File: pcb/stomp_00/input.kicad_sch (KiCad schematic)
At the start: 2 parts, among them J15 Euro_Out_1, U2 TL072

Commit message: adding all the components...
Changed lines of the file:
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@@
 (kicad_sch (version 20230121) (generator eeschema)
   (paper "A4")
+  (text_box "Input stage, usually mono, instrument level up to line level."
+    (at 111.76 21.59 0) (size 50.8 20.32)
+    (stroke (width 0) (type default))
+    (fill (type none))
+    (effects (font (size 1.27 1.27)) (justify left top))
+  )
   (global_label "LINE_IN_R" (shape input) (at 135.89 63.5 0) (fields_autoplaced)
     (effects (font (size 1.27 1.27)) (justify left))

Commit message: taking shape...
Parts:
- U2: footprint (none) -> Package_SO:SOIC-8_3.9x4.9mm_P1.27mm
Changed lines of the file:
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@@
       (effects (font (size 1.27 1.27)))
     )
-    (property "Footprint" "" (at 86.995 64.77 0)
+    (property "Footprint" "Package_SO:SOIC-8_3.9x4.9mm_P1.27mm" (at 86.995 64.77 0)
       (effects (font (size 1.27 1.27)) hide)
     )
@@
       (effects (font (size 1.27 1.27)) (justify left))
     )
-    (property "Footprint" "" (at 88.9 84.455 0)
+    (property "Footprint" "Package_SO:SOIC-8_3.9x4.9mm_P1.27mm" (at 88.9 84.455 0)
       (effects (font (size 1.27 1.27)) hide)
     )
@@
       (effects (font (size 1.27 1.27)))
     )
-    (property "Footprint" "" (at 86.36 48.26 0)
+    (property "Footprint" "Package_SO:SOIC-8_3.9x4.9mm_P1.27mm" (at 86.36 48.26 0)
       (effects (font (size 1.27 1.27)) hide)
     )

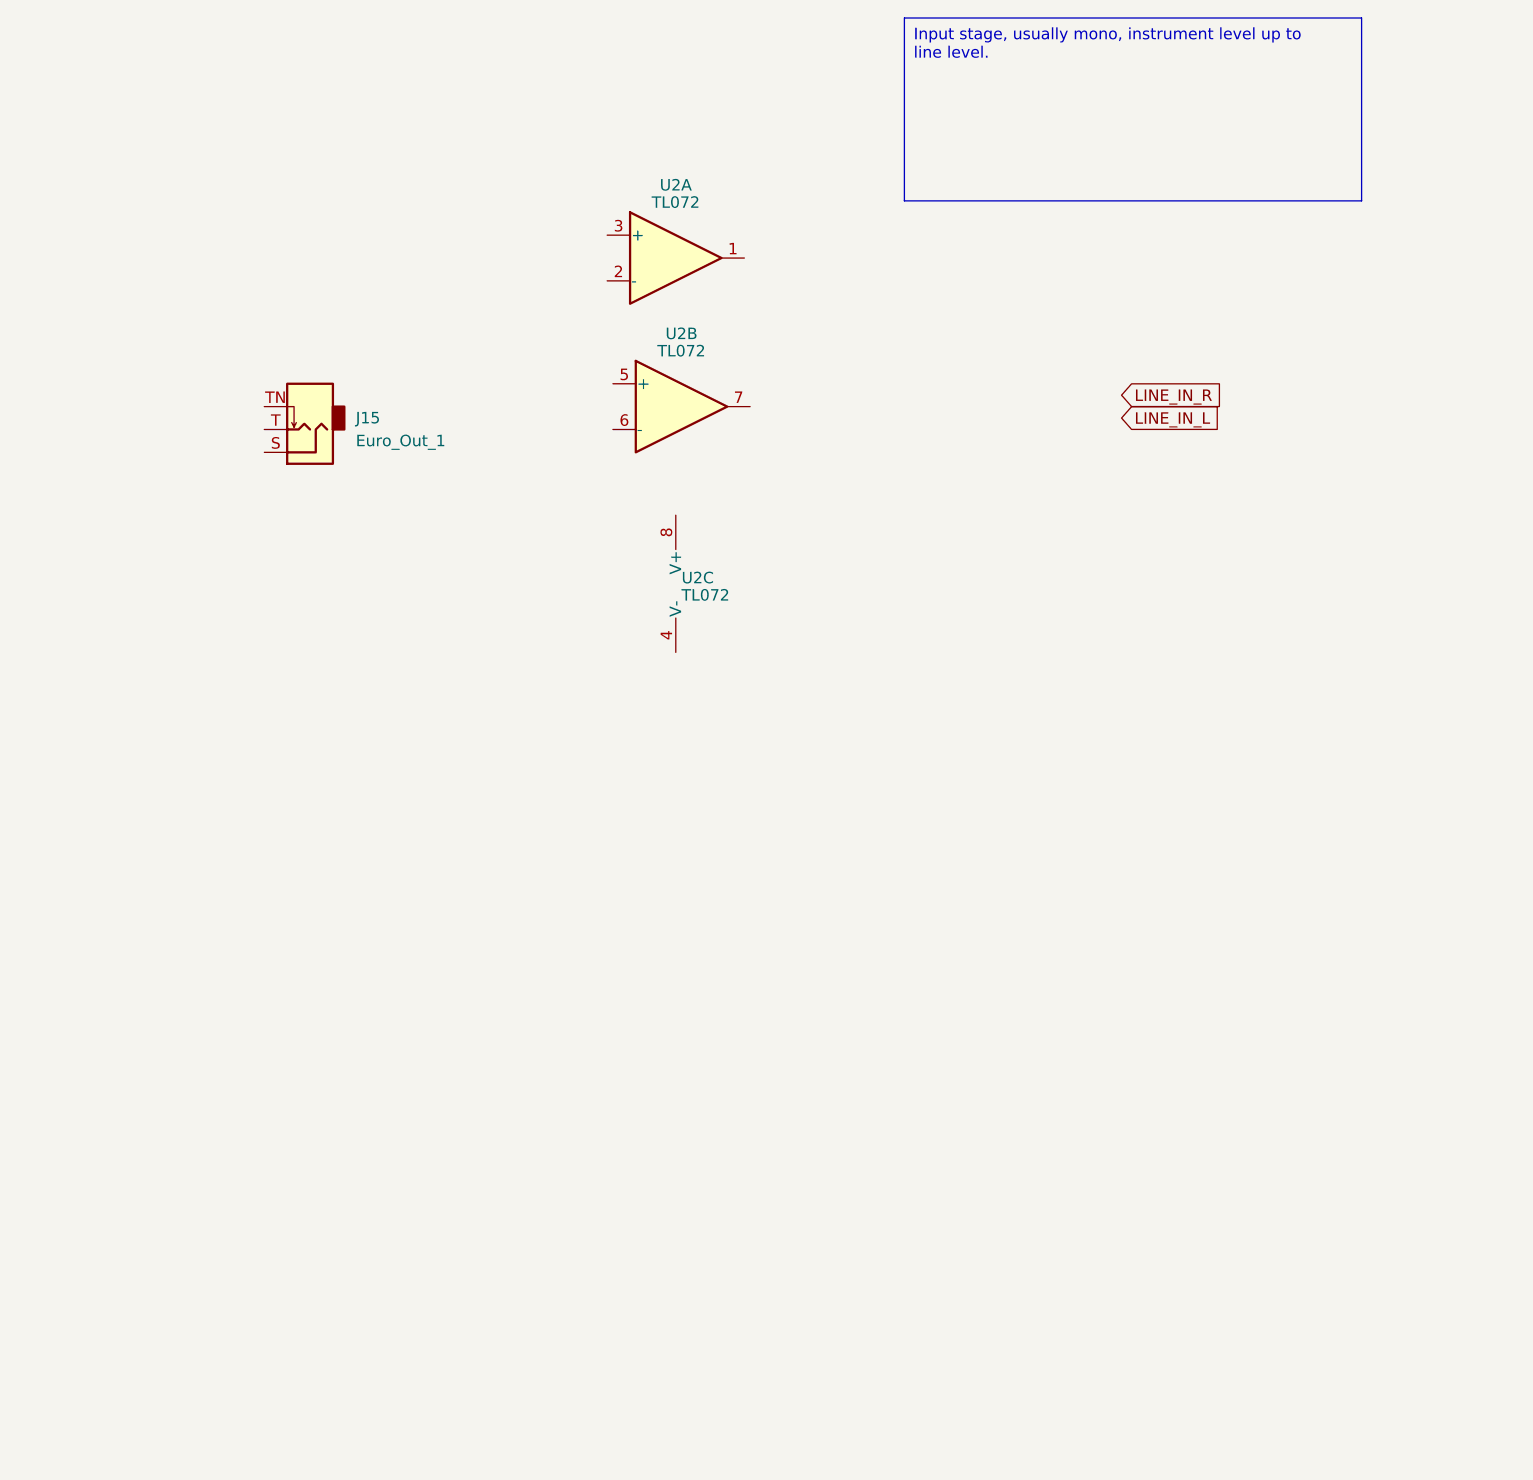
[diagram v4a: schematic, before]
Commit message: input stage schematic
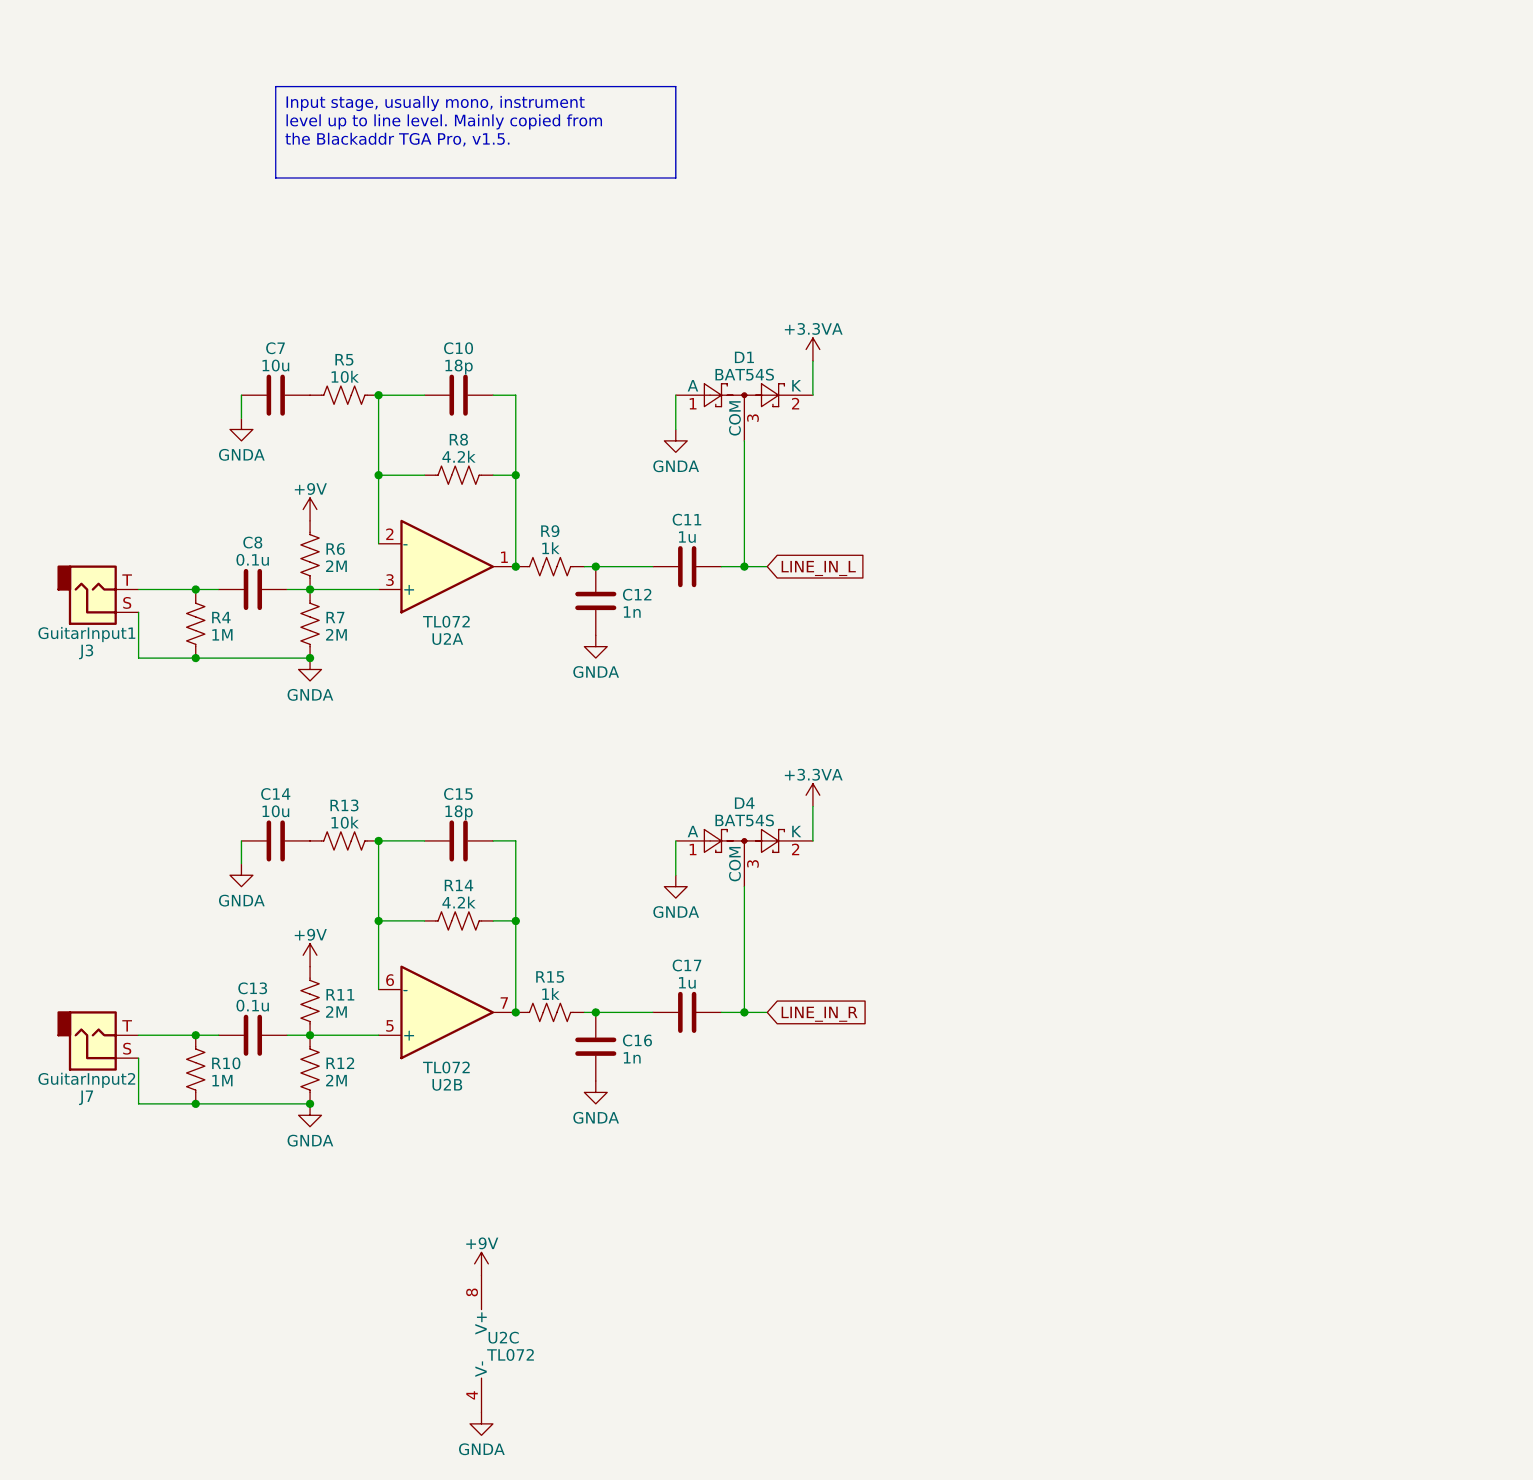
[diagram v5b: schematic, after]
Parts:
- removed J15: Euro_Out_1, AudioJacks:Jack_3.5mm_QingPu_WQP-PJ398SM_Vertical, symbol Connector_Audio:AudioJack2_SwitchT
- added C10, C15: 18p, symbol Device:C
- added C11, C17: 1u, symbol Device:C
- added C12, C16: 1n, symbol Device:C
- added C13, C8: 0.1u, symbol Device:C
- added C14, C7: 10u, symbol Device:C
- added D1, D4: BAT54S, Package_TO_SOT_SMD:SOT-23, symbol Diode:BAT54S
- added J3: GuitarInput1, symbol Connector_Audio:AudioJack2
- added J7: GuitarInput2, symbol Connector_Audio:AudioJack2
- added R10, R4: 1M, symbol Device:R_US
- added R11, R12, R6, R7: 2M, symbol Device:R_US
- added R13, R5: 10k, symbol Device:R_US
- added R14, R8: 4.2k, symbol Device:R_US
- added R15, R9: 1k, symbol Device:R_US
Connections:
- net LINE_IN_L: now also C11.1, D1.3 (COM)
- net LINE_IN_R: now also C17.1, D4.3 (COM)
- net at U2.5 (+): now also C13.2, R11.2, R12.1
- net at U2.6 (-): now also C15.1, R13.2, R14.1
- net at U2.7: now also C15.2, R14.2, R15.1
- net GNDA: now reaches U2.4 (V-)
- net GNDA: now also C12.2, C14.1, C16.2, C7.1, D1.1 (A), D4.1 (A), J3.S, J7.S, R10.2, R12.2, R4.2, R7.2
- net +9V: now reaches U2.8 (V+)
- net +9V: now also R11.1, R6.1
- net at U2.1: now also C10.2, R8.2, R9.1
- net at U2.2 (-): now also C10.1, R5.2, R8.1
- net at U2.3 (+): now also C8.2, R6.2, R7.1
- new net: C11.2, C12.1, R9.2
- new net: C14.2, R13.1
- new net: C7.2, R5.1
- new net: C16.1, C17.2, R15.2
- new net: C8.1, J3.T, R4.1
- new net: C13.1, J7.T, R10.1
- new net +3.3VA: D1.2 (K), D4.2 (K)
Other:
- moved on the sheet: U2A, U2B, U2C

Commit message: more input stage faffing
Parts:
- added C18: 100n, symbol Device:C
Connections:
- net +9V: now also C18.2
- net GNDA: now also C18.1
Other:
- note added: "Drain, prevents pop when switching to bypass"
- moved on the sheet: C10, C11, C12, C13, C14, C15, C16, C17, C7, C8, D1, D4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

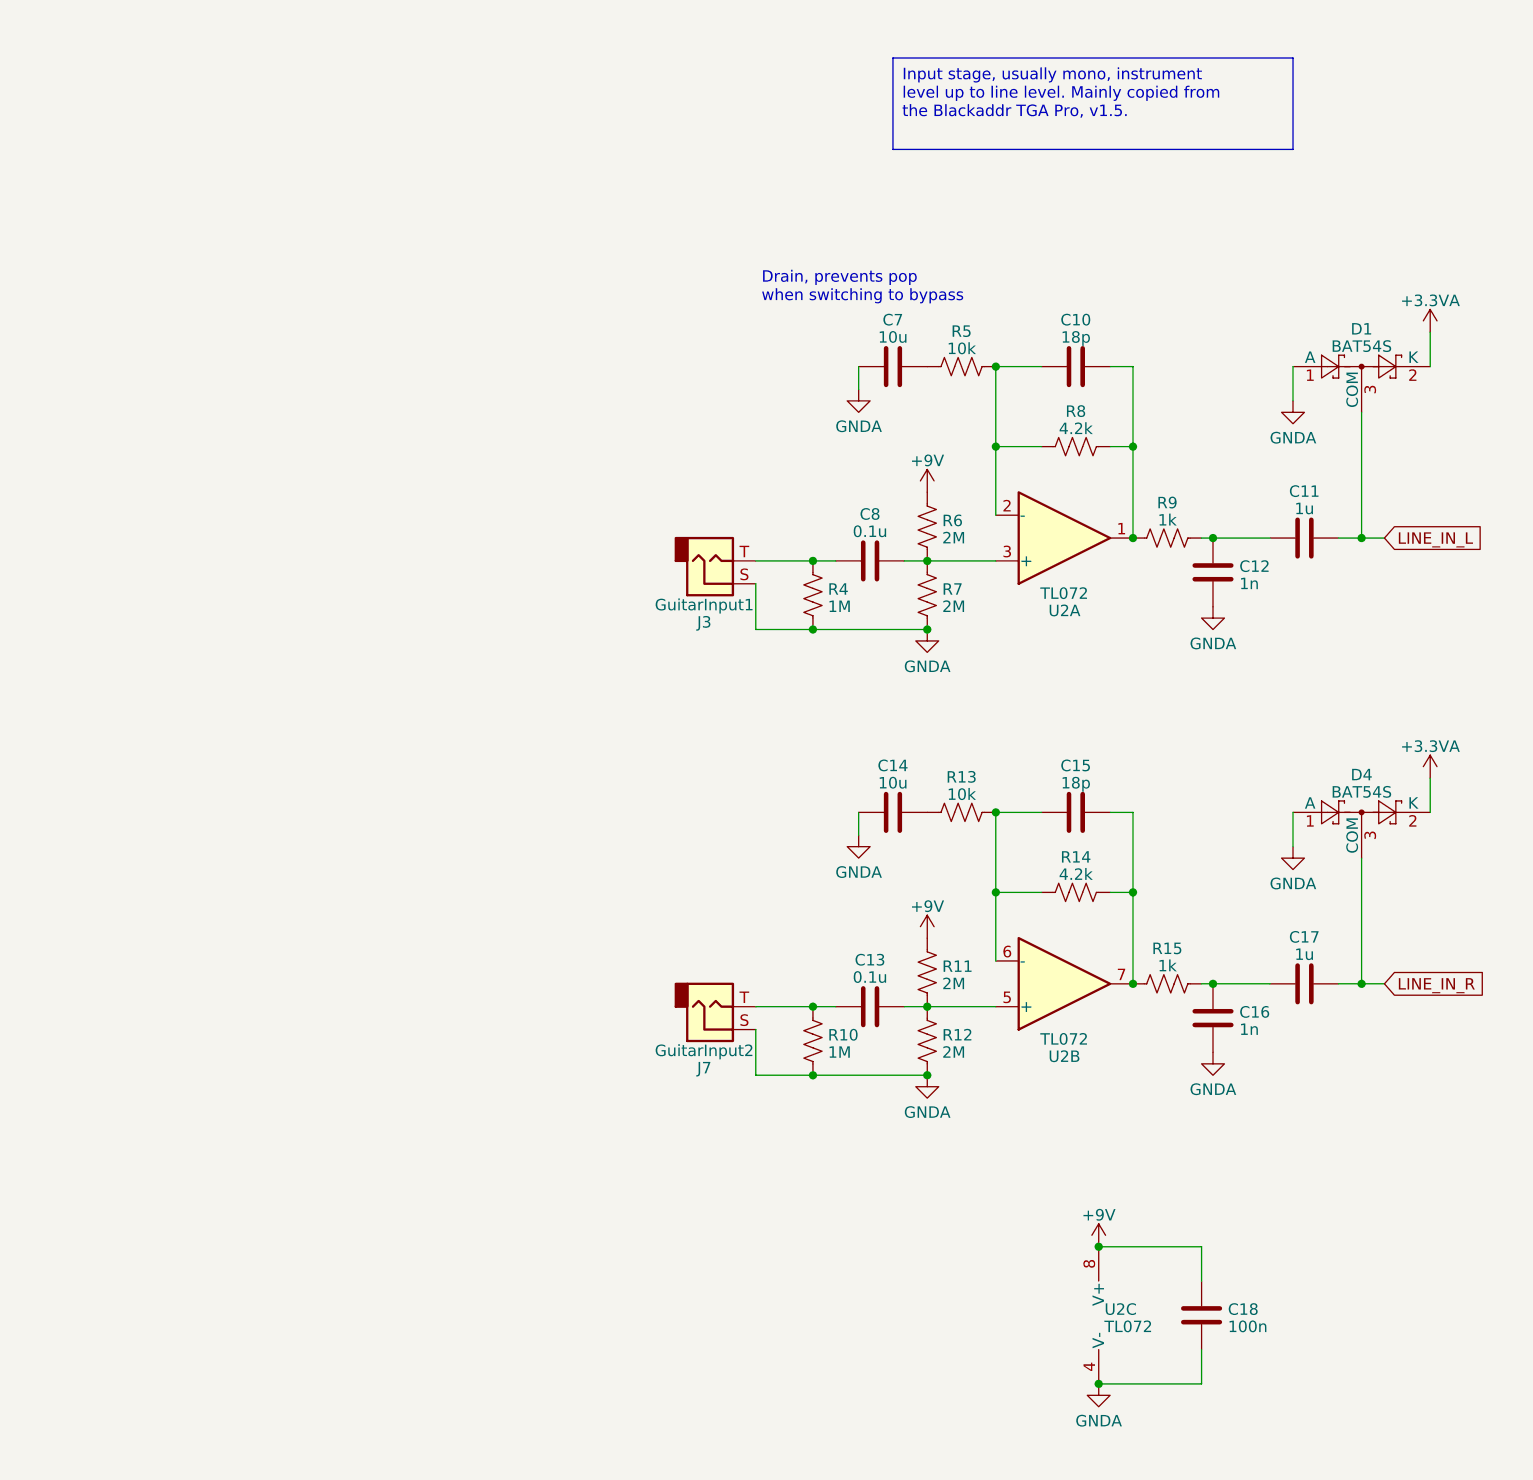
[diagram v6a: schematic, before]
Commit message: better layout in enclosure
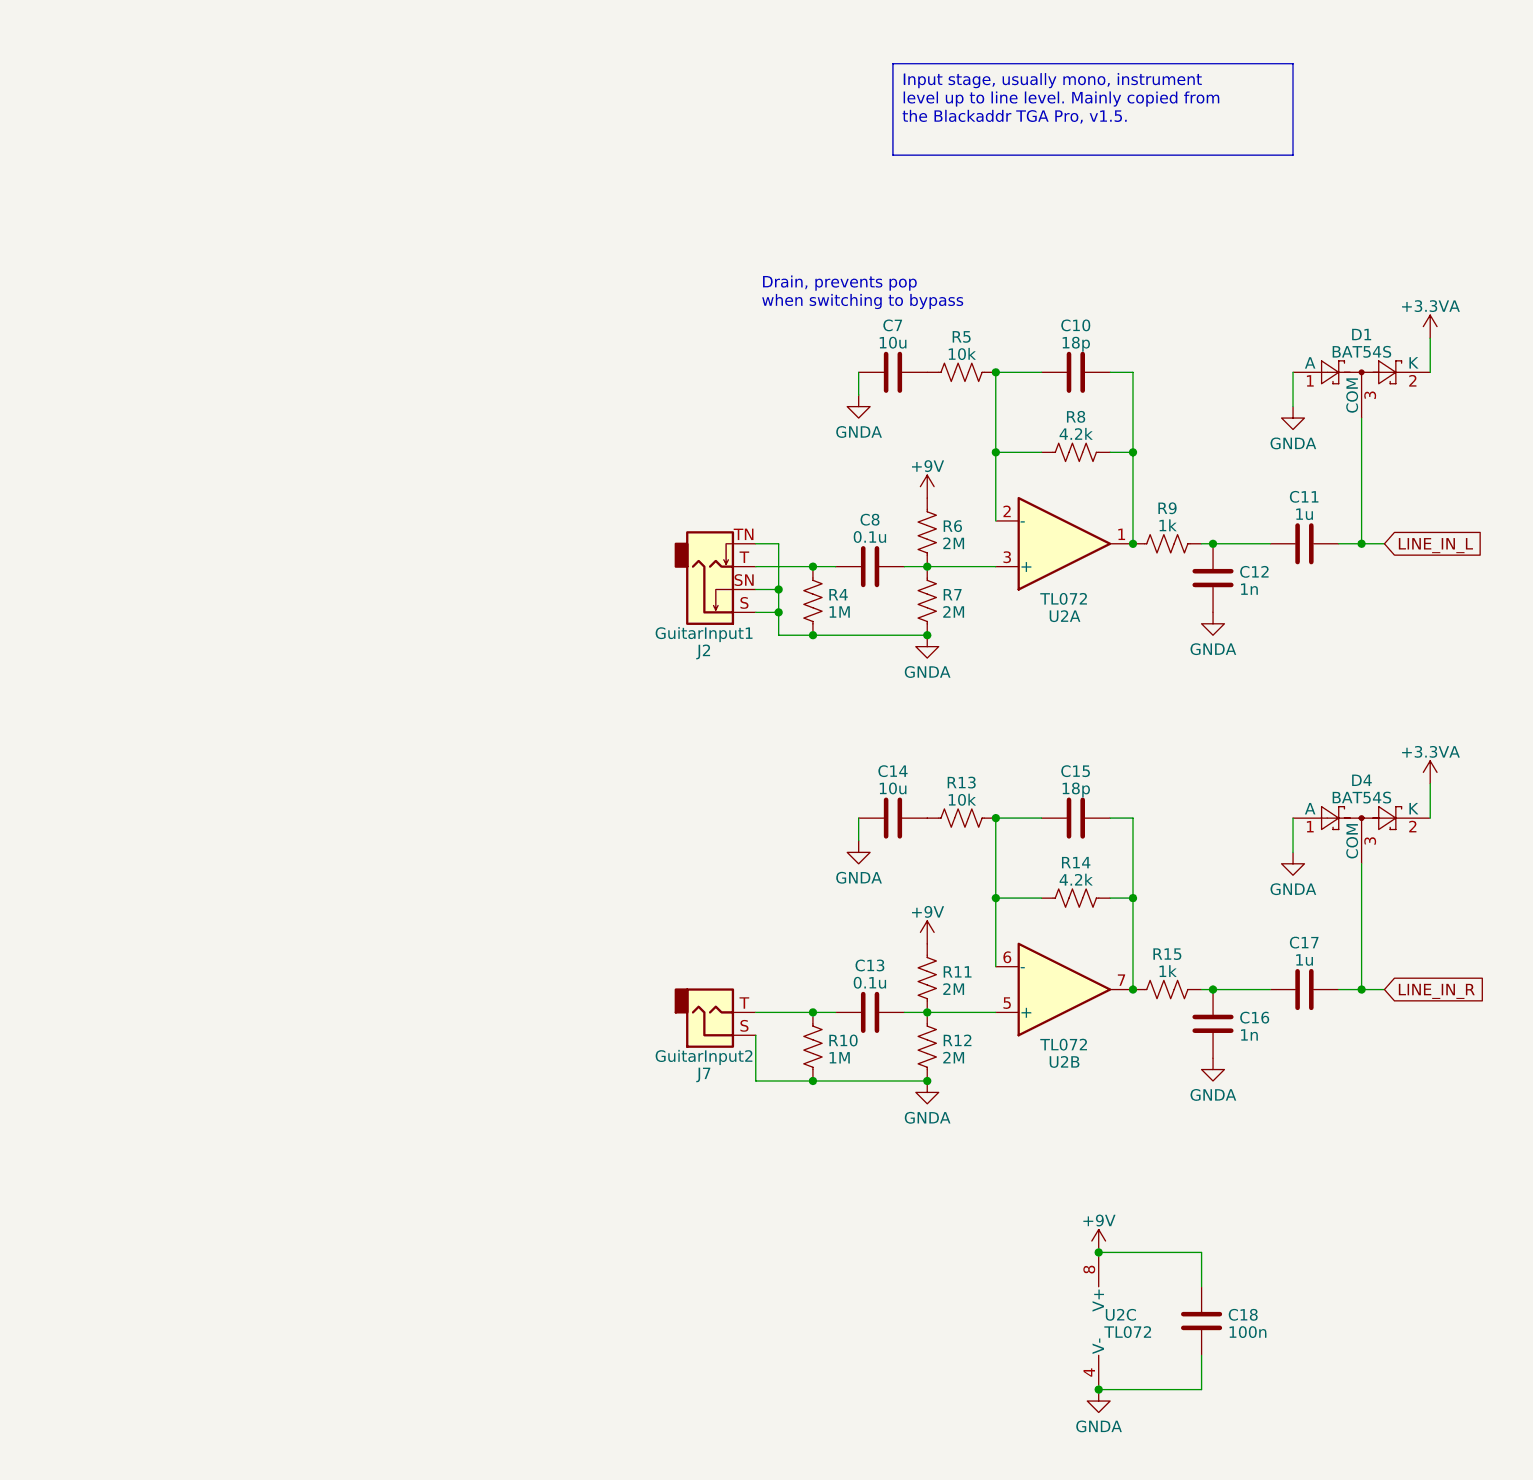
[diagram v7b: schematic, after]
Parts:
- removed J3: GuitarInput1, symbol Connector_Audio:AudioJack2
- added J2: GuitarInput1, Connector_Audio:Jack_6.35mm_Neutrik_NMJ4HCD2_Horizontal, symbol Connector_Audio:NMJ4HCD2
- J7: footprint (none) -> Connector_PinHeader_2.54mm:PinHeader_1x02_P2.54mm_Vertical
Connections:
- net GNDA: now also J2.S, J2.SN, J2.TN
- net at C8.1, R4.1: now also J2.T
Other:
- moved on the sheet: C10, C11, C12, C13, C14, C15, C16, C17, C18, C7, C8, D1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
